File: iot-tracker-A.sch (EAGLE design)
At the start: 23 parts, among them U1 ESP-WROOM-02, U2 TPL5111DDCR, U3 TPS61021ADSGR

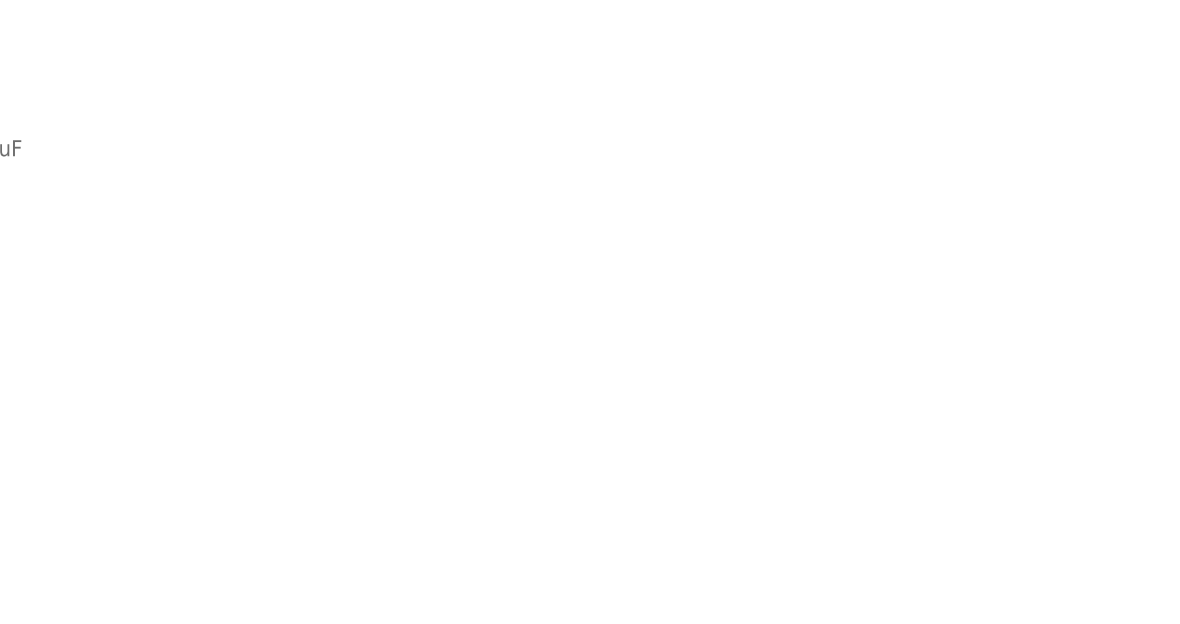
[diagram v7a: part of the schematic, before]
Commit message: Started integrating the RTC
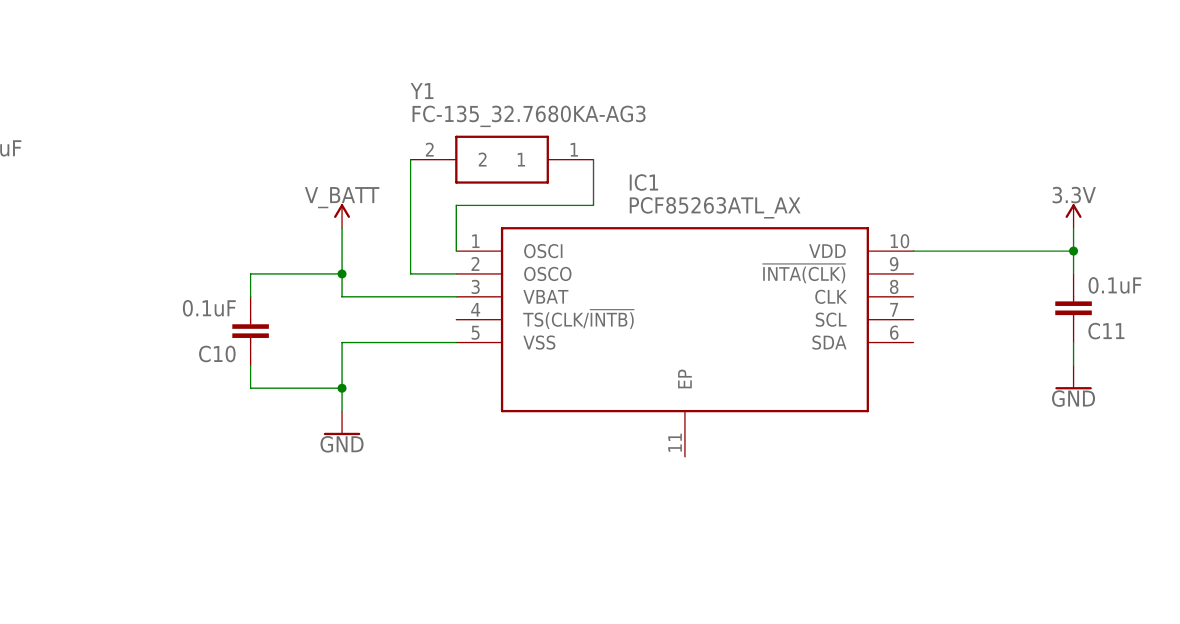
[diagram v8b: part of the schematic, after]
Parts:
- added C10, C11: 0.1uF, SparkFun-Capacitors:0.1UF-0603-25V-(+80/-20%)
- added IC1: PCF85263ATL_AX, IOT-Tracker-A:PCF85263ATL_AX
- added Y1: FC-135_32.7680KA-AG3, IOT-Tracker-A:FC-135_32.7680KA-AG3
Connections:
- new net OSCI: IC1.OSCI, Y1.1
- new net OSCO: IC1.OSCO, Y1.2
- net 3.3V: now also C11.2, IC1.VDD
- net GND: now also C10.1, C11.1, IC1.VSS
- net V_BATT: now also C10.2, IC1.VBAT
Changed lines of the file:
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@@
 <part name="R3" library="SparkFun-Resistors" library_urn="urn:adsk.eagle:library:532" deviceset="1KOHM" device="-0603-1/10W-1%" package3d_urn="urn:adsk.eagle:package:39650/1" value="1k"/>
 <part name="C6" library="SparkFun-Capacitors" library_urn="urn:adsk.eagle:library:510" deviceset="10UF" device="-0603-6.3V-20%" package3d_urn="urn:adsk.eagle:package:37414/1" value="10uF"/>
+<part name="IC1" library="IOT-Tracker-A" deviceset="PCF85263ATL_AX" device=""/>
+<part name="Y1" library="IOT-Tracker-A" deviceset="FC-135_32.7680KA-AG3" device=""/>
+<part name="SUPPLY1" library="SparkFun-PowerSymbols" library_urn="urn:adsk.eagle:library:530" deviceset="V_BATT" device=""/>
+<part name="GND7" library="SparkFun-PowerSymbols" library_urn="urn:adsk.eagle:library:530" deviceset="GND" device=""/>
+<part name="SUPPLY4" library="SparkFun-PowerSymbols" library_urn="urn:adsk.eagle:library:530" deviceset="3.3V" device=""/>
+<part name="C10" library="SparkFun-Capacitors" deviceset="0.1UF" device="-0603-25V-(+80/-20%)" value="0.1uF"/>
+<part name="C11" library="SparkFun-Capacitors" deviceset="0.1UF" device="-0603-25V-(+80/-20%)" value="0.1uF"/>
+<part name="GND9" library="SparkFun-PowerSymbols" library_urn="urn:adsk.eagle:library:530" deviceset="GND" device=""/>
 </parts>
 <sheets>
@@
 <attribute name="NAME" x="-1.016" y="35.941" size="1.778" layer="95" font="vector"/>
 <attribute name="VALUE" x="-1.016" y="30.861" size="1.778" layer="96" font="vector"/>
+</instance>
+<instance part="IC1" gate="G$1" x="152.4" y="35.56" smashed="yes">
+<attribute name="NAME" x="171.45" y="43.18" size="1.778" layer="95" align="center-left"/>
+<attribute name="VALUE" x="171.45" y="40.64" size="1.778" layer="96" align="center-left"/>
+</instance>
+<instance part="Y1" gate="G$1" x="167.64" y="45.72" smashed="yes" rot="R180">
+<attribute name="NAME" x="147.32" y="53.34" size="1.778" layer="95" align="center-left"/>
+<attribute name="VALUE" x="147.32" y="50.8" size="1.778" layer="96" align="center-left"/>
+</instance>
+<instance part="SUPPLY1" gate="G$1" x="139.7" y="38.1" smashed="yes">
+<attribute name="VALUE" x="139.7" y="40.894" size="1.778" layer="96" align="bottom-center"/>
+</instance>
+<instance part="GND7" gate="1" x="139.7" y="15.24" smashed="yes" rot="MR0">
+<attribute name="VALUE" x="139.7" y="14.986" size="1.778" layer="96" rot="MR0" align="top-center"/>
+</instance>
+<instance part="SUPPLY4" gate="G$1" x="220.98" y="38.1" smashed="yes">
+<attribute name="VALUE" x="220.98" y="40.894" size="1.778" layer="96" align="bottom-center"/>
+</instance>
+<instance part="C10" gate="G$1" x="129.54" y="27.94" smashed="yes" rot="R180">
+<attribute name="NAME" x="128.016" y="25.019" size="1.778" layer="95" font="vector" rot="R180"/>
+<attribute name="VALUE" x="128.016" y="30.099" size="1.778" layer="96" font="vector" rot="R180"/>
+</instance>
+<instance part="C11" gate="G$1" x="220.98" y="30.48" smashed="yes" rot="MR180">
+<attribute name="NAME" x="222.504" y="27.559" size="1.778" layer="95" font="vector" rot="MR180"/>
+<attribute name="VALUE" x="222.504" y="32.639" size="1.778" layer="96" font="vector" rot="MR180"/>
+</instance>
+<instance part="GND9" gate="1" x="220.98" y="20.32" smashed="yes" rot="MR0">
+<attribute name="VALUE" x="220.98" y="20.066" size="1.778" layer="96" rot="MR0" align="top-center"/>
 </instance>
 </instances>
@@
 <wire x1="-71.12" y1="12.7" x2="-71.12" y2="7.62" width="0.1524" layer="91"/>
 <pinref part="GND6" gate="1" pin="GND"/>
+</segment>
+<segment>
+<pinref part="IC1" gate="G$1" pin="VSS"/>
+<pinref part="GND7" gate="1" pin="GND"/>
+<wire x1="152.4" y1="25.4" x2="139.7" y2="25.4" width="0.1524" layer="91"/>
+<wire x1="139.7" y1="25.4" x2="139.7" y2="20.32" width="0.1524" layer="91"/>
+<pinref part="C10" gate="G$1" pin="1"/>
+<wire x1="139.7" y1="20.32" x2="139.7" y2="17.78" width="0.1524" layer="91"/>
+<wire x1="129.54" y1="22.86" x2="129.54" y2="20.32" width="0.1524" layer="91"/>
+<wire x1="129.54" y1="20.32" x2="139.7" y2="20.32" width="0.1524" layer="91"/>
+<junction x="139.7" y="20.32"/>
+</segment>
+<segment>
+<pinref part="C11" gate="G$1" pin="1"/>
+<pinref part="GND9" gate="1" pin="GND"/>
+<wire x1="220.98" y1="25.4" x2="220.98" y2="22.86" width="0.1524" layer="91"/>
 </segment>
 </net>
@@
 <pinref part="C9" gate="G$1" pin="2"/>
 </segment>
+<segment>
+<pinref part="IC1" gate="G$1" pin="VDD"/>
+<pinref part="C11" gate="G$1" pin="2"/>
+<wire x1="203.2" y1="35.56" x2="220.98" y2="35.56" width="0.1524" layer="91"/>
+<wire x1="220.98" y1="35.56" x2="220.98" y2="33.02" width="0.1524" layer="91"/>
+<pinref part="SUPPLY4" gate="G$1" pin="3.3V"/>
+<wire x1="220.98" y1="38.1" x2="220.98" y2="35.56" width="0.1524" layer="91"/>
+<junction x="220.98" y="35.56"/>
+</segment>
 </net>
 <net name="V_BATT" class="1">
@@
 <pinref part="C6" gate="G$1" pin="1"/>
 </segment>
+<segment>
+<pinref part="IC1" gate="G$1" pin="VBAT"/>
+<wire x1="152.4" y1="30.48" x2="139.7" y2="30.48" width="0.1524" layer="91"/>
+<pinref part="SUPPLY1" gate="G$1" pin="V_BATT"/>
+<wire x1="139.7" y1="30.48" x2="139.7" y2="33.02" width="0.1524" layer="91"/>
+<pinref part="C10" gate="G$1" pin="2"/>
+<wire x1="139.7" y1="33.02" x2="139.7" y2="38.1" width="0.1524" layer="91"/>
+<wire x1="129.54" y1="30.48" x2="129.54" y2="33.02" width="0.1524" layer="91"/>
+<wire x1="129.54" y1="33.02" x2="139.7" y2="33.02" width="0.1524" layer="91"/>
+<junction x="139.7" y="33.02"/>
+</segment>
 </net>
 <net name="IO4_LED" class="0">
@@
 </segment>
 </net>
+<net name="OSCI" class="0">
+<segment>
+<pinref part="Y1" gate="G$1" pin="1"/>
+<wire x1="167.64" y1="45.72" x2="167.64" y2="40.64" width="0.1524" layer="91"/>
+<wire x1="167.64" y1="40.64" x2="152.4" y2="40.64" width="0.1524" layer="91"/>
+<pinref part="IC1" gate="G$1" pin="OSCI"/>
+<wire x1="152.4" y1="40.64" x2="152.4" y2="35.56" width="0.1524" layer="91"/>
+</segment>
+</net>
+<net name="OSCO" class="0">
+<segment>
+<pinref part="Y1" gate="G$1" pin="2"/>
+<pinref part="IC1" gate="G$1" pin="OSCO"/>
+<wire x1="147.32" y1="45.72" x2="147.32" y2="33.02" width="0.1524" layer="91"/>
+<wire x1="147.32" y1="33.02" x2="152.4" y2="33.02" width="0.1524" layer="91"/>
+</segment>
+</net>
